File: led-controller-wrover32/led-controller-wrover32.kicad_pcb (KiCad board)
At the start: 4 copper layers, 36 x 43 mm, 85 parts, among them J1 Micro_SD_Card, J10 Conn_01x02 DNS, J101 Conn_01x02, J11 Conn_01x02, J2 BM12B-SRSS-TBT(LF)(SN), J3 USB_B_Micro, J4 BM12B-SRSS-TBT(LF)(SN), J5 Conn_01x04 DNI, J6 Conn_01x02 DNI, J7 Conn_01x02 DNI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

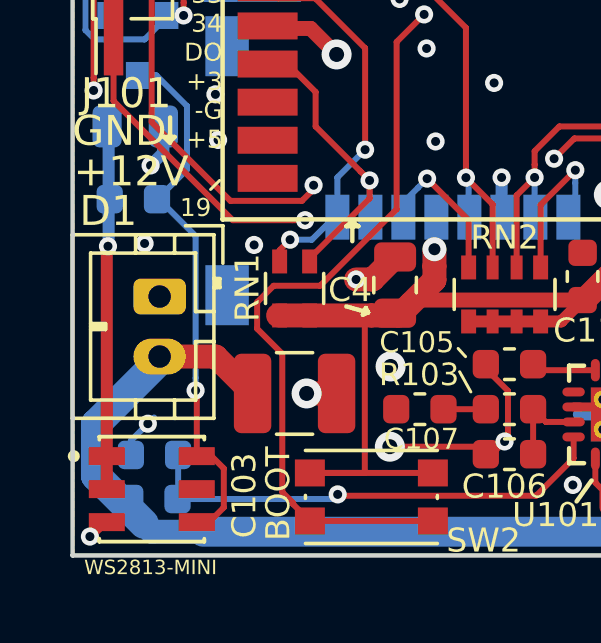
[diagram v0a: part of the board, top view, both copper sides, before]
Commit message: Moved WS2813B after fixing footprint  v3.6
Signed-off-by: Aaron Williams <aaron.w2@gmail.com>
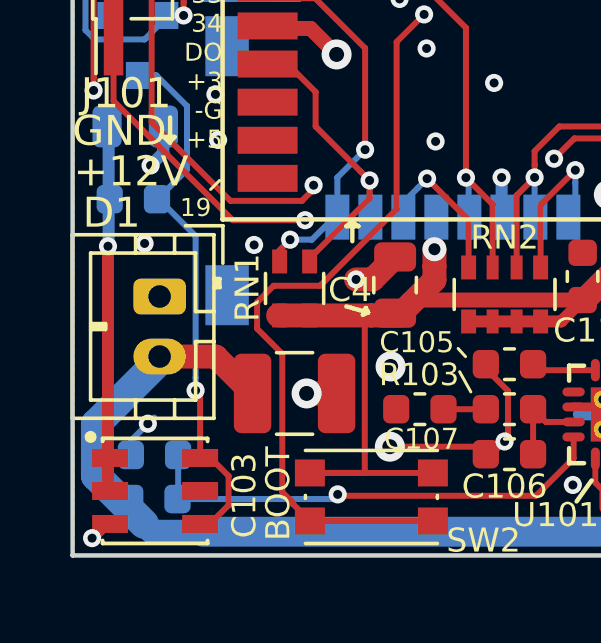
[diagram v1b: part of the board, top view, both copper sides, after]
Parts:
- C23: value 1nF -> 22nF
- FID1, FID2, FID3, FID4: value FIDUCIAL_1MM -> DNF
- J10: value Conn_01x02 DNS -> Conn_01x02 DNF
- J5: value Conn_01x04 DNI -> Conn_01x04
- J6, J7, J9: value Conn_01x02 DNI -> Conn_01x02 DNF
- J8: value Conn_01x05 DNI -> Conn_01x05 DNF
- TP1, TP2: value TestPoint -> DNF
- moved D1 0.13 mm to (52.8, 82.8)
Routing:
- net /DO: track 33.7 -> 34.2 mm
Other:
- board text added: "Rev 3.6"
- board text removed: "Rev 3.5.2"

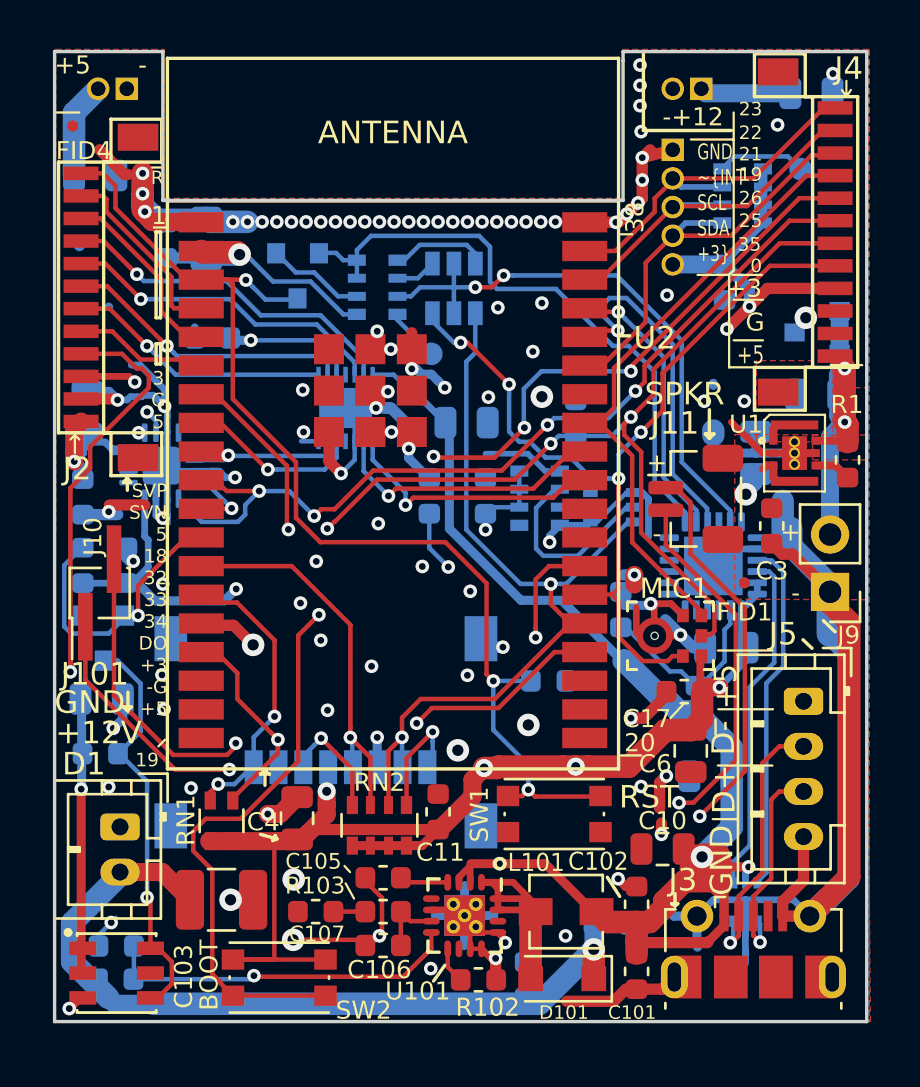
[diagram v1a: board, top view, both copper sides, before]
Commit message: Changed UART to CP2104 to simplify.
Signed-off-by: Aaron Williams <aaron.w2@gmail.com>
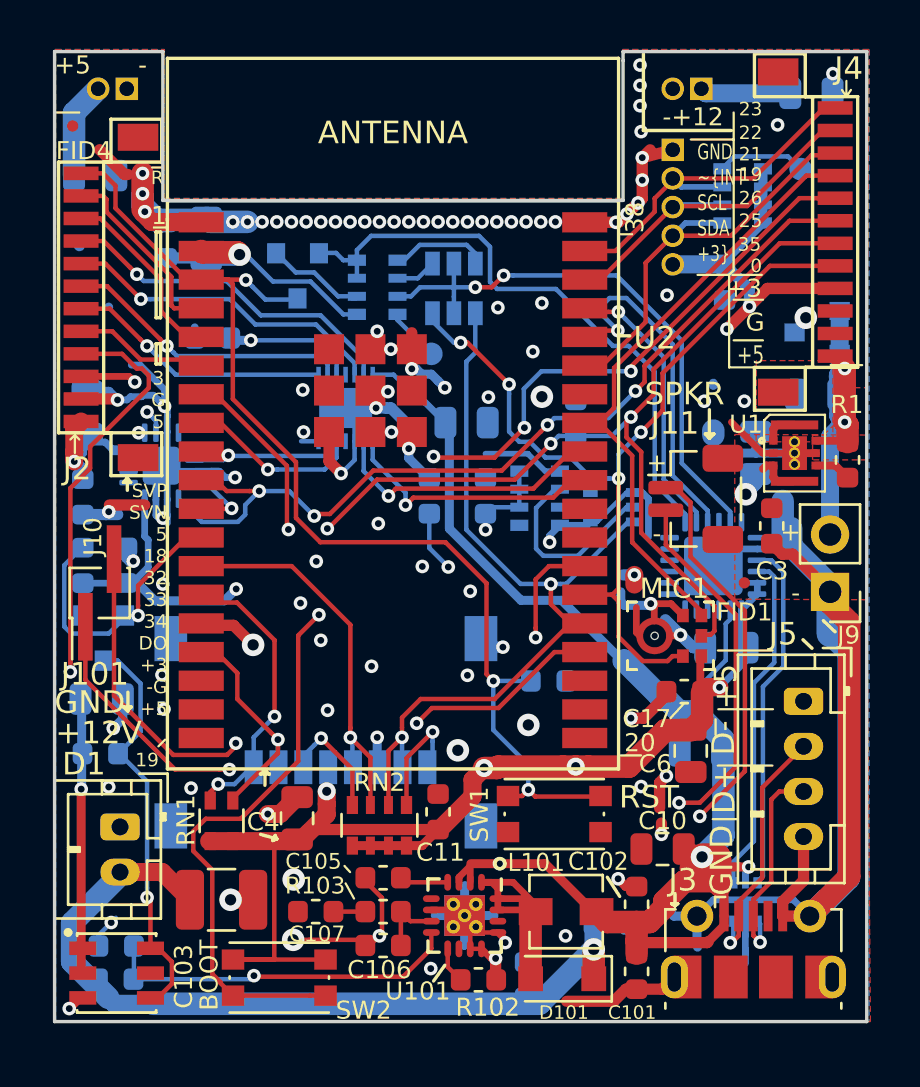
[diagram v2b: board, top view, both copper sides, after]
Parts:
- removed R12: 22.1K, Resistor_SMD:R_0603_1608Metric
- removed R13: 47.5K, Resistor_SMD:R_0603_1608Metric
- U3: value CP2102N-A01-GQFN24 -> CP2104; footprint Aaron:QFN-24-1EP_4x4mm_Pitch0.5mm_rounded_corners -> Package_DFN_QFN:QFN-24-1EP_4x4mm_P0.5mm_EP2.6x2.6mm
- moved C19 1.20 mm to (78.7, 73.0)
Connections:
- U3 pad 8: /VBUS_REF -> VBUS
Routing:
- net /VBUS_REF: track 8.58 -> 0.00 mm
- net VBUS: track 100.8 -> 105.7 mm
- net /D-: track 11.7 -> 11.1 mm
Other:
- board text added: "Rev 3.7"
- board text removed: "Rev 3.6"

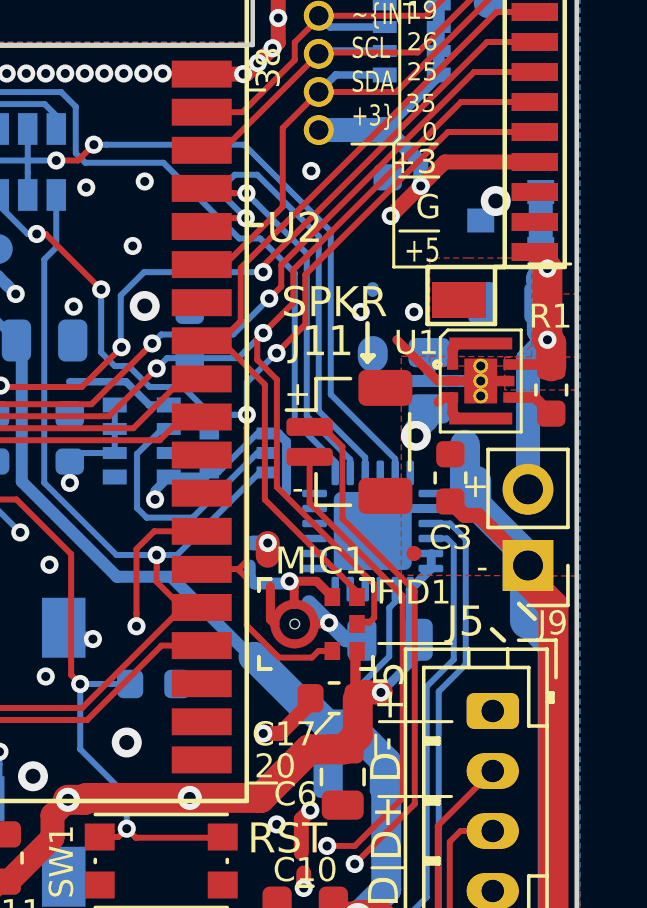
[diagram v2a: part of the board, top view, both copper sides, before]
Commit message: Minor changes
- Tweaked some of the component values in the 12V supply as per TI.
- Removed unnecessary protection diode, the USB one is enough.
- Changed UART to CS2104 which eliminates two resistors and is
  slightly cheaper
- Updated PCB to reflect changes.

Signed-off-by: Aaron Williams <aaron.w2@gmail.com>
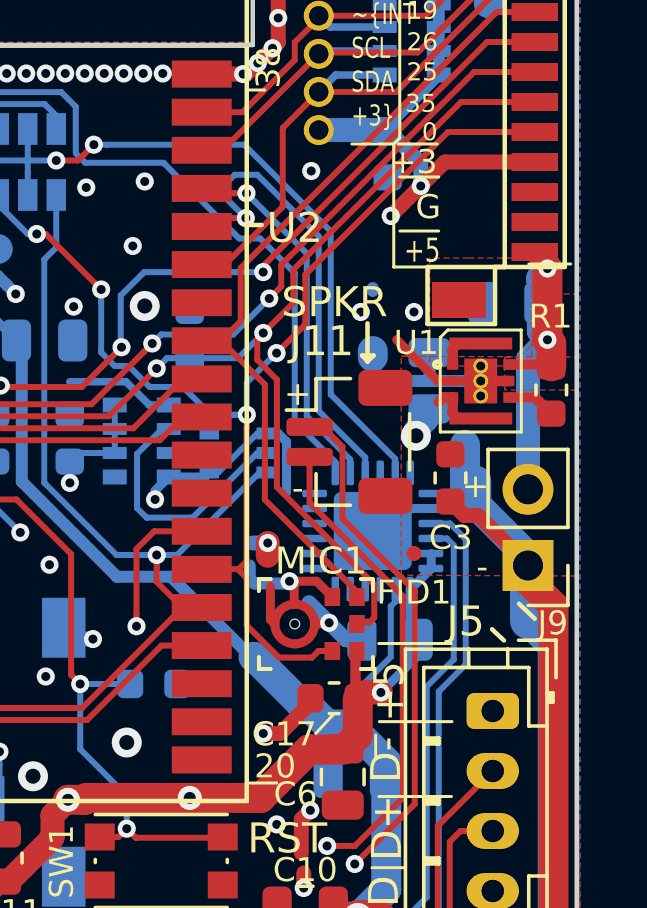
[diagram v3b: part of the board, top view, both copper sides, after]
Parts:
- removed D3: SP0502BAHT, Package_TO_SOT_SMD:SOT-23
- C101: value 6.8uF -> 22uF
- C103: value 22uF -> 47uF
- R102: value 18.2K -> 18.7K
- R103: value 1.69K -> 1.62K
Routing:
- net VBUS: track 105.7 -> 102.8 mm
- net GND: vias 101 -> 100
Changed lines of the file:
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@@
     (thickness 1.6)
     (drawings 142)
-    (tracks 1327)
+    (tracks 1324)
     (zones 0)
-    (modules 83)
+    (modules 82)
     (nets 88)
   )
@@
     )
   )
-  (module Package_TO_SOT_SMD:SOT-23 (layer B.Cu)
-    (at 83.8 54.45 180)
-    (descr "SOT-23, Standard")
-    (tags SOT-23)
-    (attr smd)
-    (fp_text reference D3 (at 1.758 1.618) (layer B.SilkS)
-      (effects (font (size 1 1) (thickness 0.15)) (justify mirror))
-    )
-    (fp_text value SP0502BAHT (at -5.0365 -0.033) (layer B.Fab)
-      (effects (font (size 0.6 0.6) (thickness 0.1)) (justify mirror))
-    )
-    (fp_line (start 0.76 -1.58) (end -0.7 -1.58) (layer B.SilkS) (width 0.12))
-    (fp_line (start 0.76 1.58) (end -1.4 1.58) (layer B.SilkS) (width 0.12))
-    (fp_line (start -1.7 -1.75) (end -1.7 1.75) (layer B.CrtYd) (width 0.05))
-    (fp_line (start 1.7 -1.75) (end -1.7 -1.75) (layer B.CrtYd) (width 0.05))
-    (fp_line (start 1.7 1.75) (end 1.7 -1.75) (layer B.CrtYd) (width 0.05))
-    (fp_line (start -1.7 1.75) (end 1.7 1.75) (layer B.CrtYd) (width 0.05))
-    (fp_line (start 0.76 1.58) (end 0.76 0.65) (layer B.SilkS) (width 0.12))
-    (fp_line (start 0.76 -1.58) (end 0.76 -0.65) (layer B.SilkS) (width 0.12))
-    (fp_line (start -0.7 -1.52) (end 0.7 -1.52) (layer B.Fab) (width 0.1))
-    (fp_line (start 0.7 1.52) (end 0.7 -1.52) (layer B.Fab) (width 0.1))
-    (fp_line (start -0.7 0.95) (end -0.15 1.52) (layer B.Fab) (width 0.1))
-    (fp_line (start -0.15 1.52) (end 0.7 1.52) (layer B.Fab) (width 0.1))
-    (fp_line (start -0.7 0.95) (end -0.7 -1.5) (layer B.Fab) (width 0.1))
-    (fp_text user %R (at 0 0 -90) (layer B.Fab)
-      (effects (font (size 0.5 0.5) (thickness 0.075)) (justify mirror))
-    )
-    (pad 3 smd rect (at 1 0 180) (size 0.9 0.8) (layers B.Cu B.Paste B.Mask)
-      (net 2 GND))
-    (pad 2 smd rect (at -1 -0.95 180) (size 0.9 0.8) (layers B.Cu B.Paste B.Mask)
-      (net 1 VBUS))
-    (pad 1 smd rect (at -1 0.95 180) (size 0.9 0.8) (layers B.Cu B.Paste B.Mask)
-      (net 1 VBUS))
-    (model ${KISYS3DMOD}/Package_TO_SOT_SMD.3dshapes/SOT-23.wrl
-      (at (xyz 0 0 0))
-      (scale (xyz 1 1 1))
-      (rotate (xyz 0 0 0))
-    )
-  )
   (module Package_TO_SOT_SMD:SOT-363_SC-70-6 (layer B.Cu)
     (at 74.7 62.2)
@@
       (effects (font (size 0.6 0.6) (thickness 0.1)))
     )
-    (fp_text value 6.8uF (at 2.569 -0.019 270) (layer F.Fab)
+    (fp_text value 22uF (at 2.569 -0.019 270) (layer F.Fab)
       (effects (font (size 0.6 0.6) (thickness 0.1)))
     )
@@
       (effects (font (size 0.8 0.8) (thickness 0.1)))
     )
-    (fp_text value 22uF (at -1.2 2.28) (layer F.Fab)
+    (fp_text value 47uF (at -1.2 2.28) (layer F.Fab)
       (effects (font (size 1 1) (thickness 0.15)))
     )
@@
       (effects (font (size 0.8 0.8) (thickness 0.15)))
     )
-    (fp_text value 18.2K (at 0.0465 1.2415) (layer F.Fab)
+    (fp_text value 18.7K (at 0.0465 1.2415) (layer F.Fab)
       (effects (font (size 0.6 0.6) (thickness 0.1)))
     )
@@
       (effects (font (size 0.75 0.75) (thickness 0.12)))
     )
-    (fp_text value 1.69K (at 1.4375 0.075 90) (layer F.Fab)
+    (fp_text value 1.62K (at 1.4375 0.075 90) (layer F.Fab)
       (effects (font (size 0.6 0.6) (thickness 0.1)))
     )
@@
   (via (at 69.72 78) (size 0.604) (drill 0.3) (layers F.Cu B.Cu) (net 1))
   (segment (start 84.7375 57.2) (end 84.7375 56.4625) (width 0.8) (layer B.Cu) (net 1) (status 10))
-  (segment (start 84.8 56.4) (end 84.8 53.6) (width 0.8) (layer B.Cu) (net 1))
   (segment (start 84.7375 56.4625) (end 84.8 56.4) (width 0.8) (layer B.Cu) (net 1))
-  (segment (start 84.8 53.6) (end 84.75 53.55) (width 0.8) (layer B.Cu) (net 1))
   (segment (start 67.325 58.45) (end 67.2765 58.45) (width 0.35) (layer B.Cu) (net 1))
   (segment (start 65.925 57.05) (end 67.325 58.45) (width 0.3) (layer B.Cu) (net 1))
@@
   (segment (start 51.17902 82.77902) (end 51.25 82.85) (width 0.4) (layer F.Cu) (net 1))
   (segment (start 51.17902 74.693765) (end 51.17902 82.77902) (width 0.4) (layer F.Cu) (net 1))
-  (segment (start 79.95 67.162668) (end 79.75 67.362668) (width 0.2) (layer B.Cu) (net 1))
-  (segment (start 79.95 66.7375) (end 79.95 67.162668) (width 0.2) (layer B.Cu) (net 1))
-  (segment (start 78.40001 70.331484) (end 78.40001 71.25001) (width 0.2) (layer B.Cu) (net 1))
-  (segment (start 79.75 68.981494) (end 78.40001 70.331484) (width 0.2) (layer B.Cu) (net 1))
-  (segment (start 79.75 67.362668) (end 79.75 68.981494) (width 0.2) (layer B.Cu) (net 1))
   (segment (start 79.65 76.75) (end 78.7 77.7) (width 1) (layer B.Cu) (net 1))
   (segment (start 78.40001 71.25001) (end 79.65 72.5) (width 1) (layer B.Cu) (net 1))
   (segment (start 79.65 72.5) (end 79.65 76.75) (width 1) (layer B.Cu) (net 1))
+  (segment (start 78.40001 70.39999) (end 78.40001 71.25001) (width 0.2) (layer B.Cu) (net 1))
+  (segment (start 79.8 67.312668) (end 79.8 69) (width 0.2) (layer B.Cu) (net 1))
+  (segment (start 79.95 66.7375) (end 79.95 67.162668) (width 0.2) (layer B.Cu) (net 1))
+  (segment (start 79.8 69) (end 78.40001 70.39999) (width 0.2) (layer B.Cu) (net 1))
+  (segment (start 79.95 67.162668) (end 79.8 67.312668) (width 0.2) (layer B.Cu) (net 1))
   (via (at 75.95 42.6) (size 0.604) (drill 0.3) (layers F.Cu B.Cu) (net 2))
   (via (at 52.4 74.6) (size 0.604) (drill 0.3) (layers F.Cu B.Cu) (net 2))
@@
   (segment (start 76.049988 47.7) (end 76.049988 46.705012) (width 0.5) (layer F.Cu) (net 2))
   (via (at 76.049988 47.7) (size 0.604) (drill 0.3) (layers F.Cu B.Cu) (net 2))
-  (via (at 83.3 53.8) (size 1) (drill 0.5) (layers F.Cu B.Cu) (net 2))
   (segment (start 82.075 64.05) (end 82.35 63.775) (width 0.3) (layer B.Cu) (net 2))
   (segment (start 82.075 64.05) (end 81.15 64.05) (width 0.3) (layer B.Cu) (net 2) (status 20))
